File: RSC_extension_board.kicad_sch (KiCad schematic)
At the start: 35 parts, among them J1 Conn_01x03, J10 Conn_01x02, J2 Conn_01x03, J3 Raspberry_Pi_4, J4 Conn_01x04, J5 Conn_01x03, J6 Conn_01x02, J7 Conn_01x03, J8 PRT-14417, J9 USB_C_Receptacle_PowerOnly_6P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

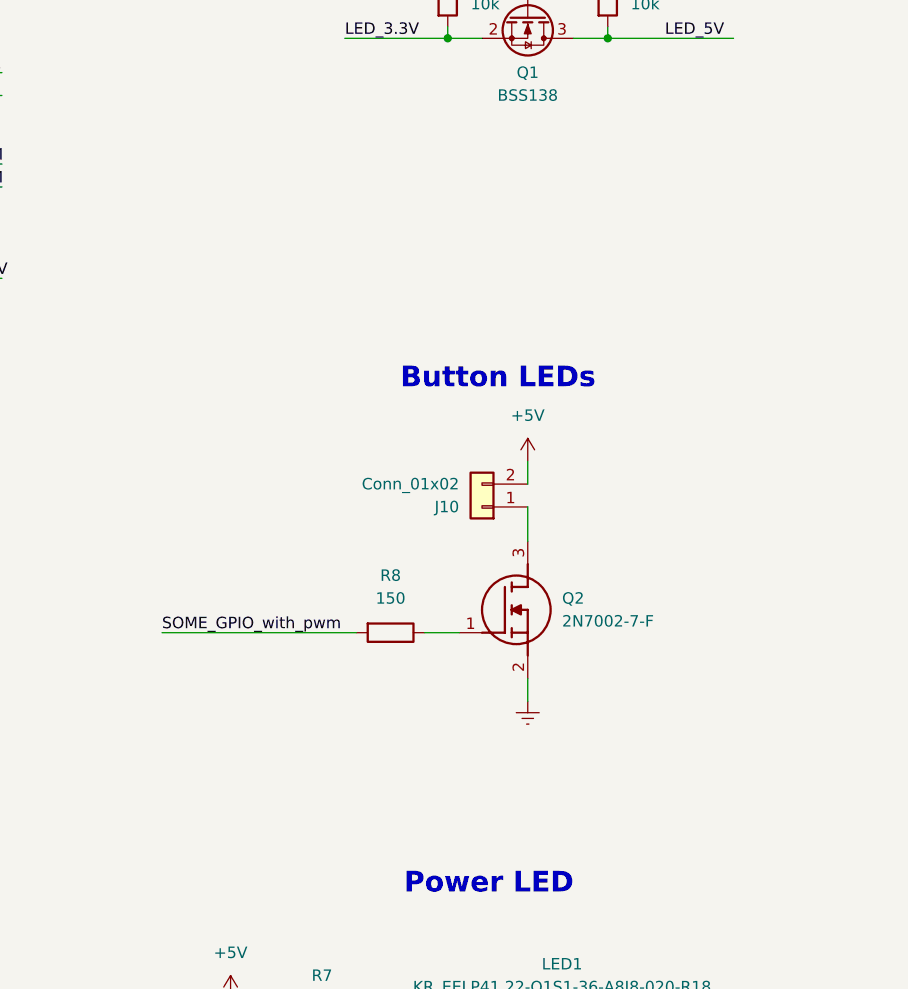
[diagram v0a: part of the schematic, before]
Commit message: started possible voice schematic
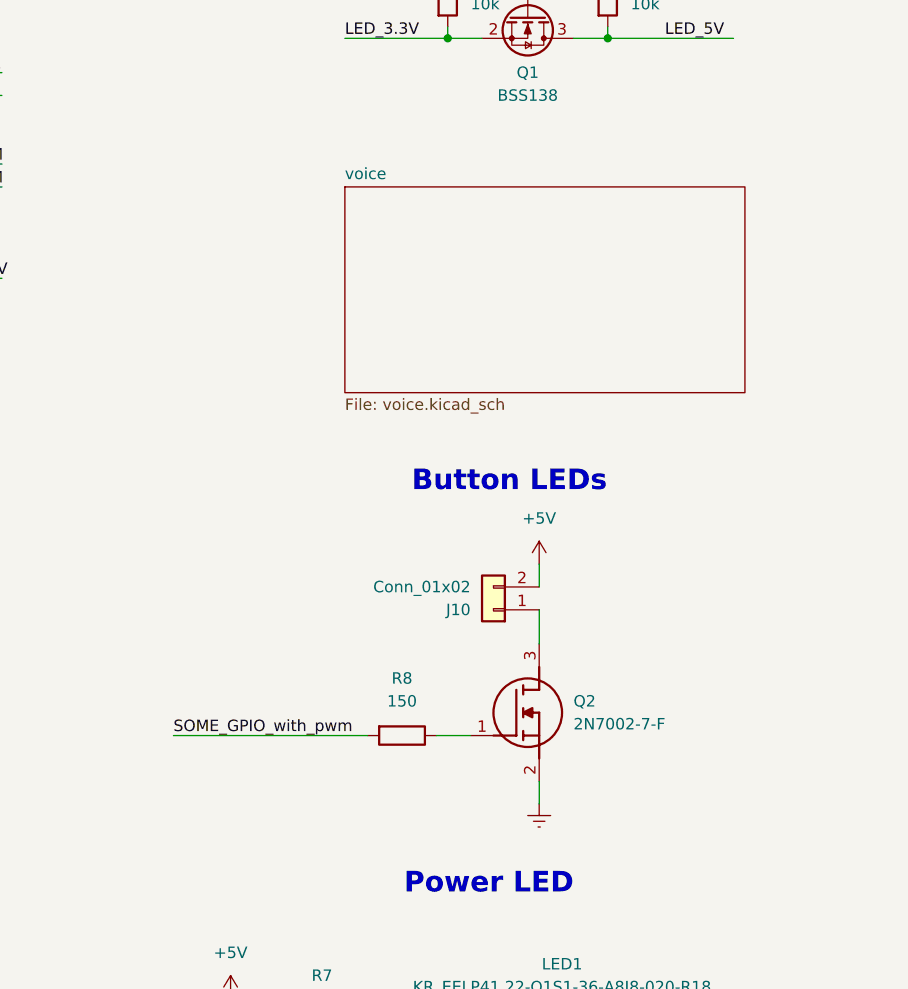
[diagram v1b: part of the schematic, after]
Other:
- added sheet voice (voice.kicad_sch)
- moved on the sheet: J10, Q2, R8
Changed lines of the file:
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@@
 	(text "Button LEDs"
 		(exclude_from_sim no)
-		(at 165.608 82.296 0)
+		(at 166.878 93.726 0)
 		(effects
 			(font
@@
 	(wire
 		(pts
-			(xy 128.27 110.49) (xy 149.86 110.49)
+			(xy 129.54 121.92) (xy 151.13 121.92)
 		)
 		(stroke
@@
 	(wire
 		(pts
-			(xy 157.48 110.49) (xy 161.29 110.49)
+			(xy 158.75 121.92) (xy 162.56 121.92)
 		)
 		(stroke
@@
 	(wire
 		(pts
-			(xy 168.91 96.52) (xy 168.91 100.33)
+			(xy 170.18 107.95) (xy 170.18 111.76)
 		)
 		(stroke
@@
 	(wire
 		(pts
-			(xy 168.91 118.11) (xy 168.91 115.57)
+			(xy 170.18 129.54) (xy 170.18 127)
 		)
 		(stroke
@@
 	(wire
 		(pts
-			(xy 168.91 91.44) (xy 168.91 93.98)
+			(xy 170.18 102.87) (xy 170.18 105.41)
 		)
 		(stroke
@@
 	)
 	(label "SOME_GPIO_with_pwm"
-		(at 128.27 110.49 0)
+		(at 129.54 121.92 0)
 		(effects
 			(font
@@
 	(symbol
 		(lib_id "power:+5V")
-		(at 168.91 91.44 0)
+		(at 170.18 102.87 0)
 		(unit 1)
 		(exclude_from_sim no)
@@
 		(fields_autoplaced yes)
 		(property "Reference" "#PWR032"
-			(at 168.91 95.25 0)
+			(at 170.18 106.68 0)
 			(effects
 				(font
@@
 		)
 		(property "Value" "+5V"
-			(at 168.91 86.36 0)
+			(at 170.18 97.79 0)
 			(effects
 				(font
@@
 		)
 		(property "Footprint" ""
-			(at 168.91 91.44 0)
+			(at 170.18 102.87 0)
 			(effects
 				(font
@@
 		)
 		(property "Datasheet" ""
-			(at 168.91 91.44 0)
+			(at 170.18 102.87 0)
 			(effects
 				(font
@@
 		)
 		(property "Description" "Power symbol creates a global label with name \"+5V\""
-			(at 168.91 91.44 0)
+			(at 170.18 102.87 0)
 			(effects
 				(font
@@
 	(symbol
 		(lib_id "Connector_Generic:Conn_01x02")
-		(at 163.83 96.52 180)
+		(at 165.1 107.95 180)
 		(unit 1)
 		(exclude_from_sim no)
@@
 		(fields_autoplaced yes)
 		(property "Reference" "J10"
-			(at 161.29 96.5201 0)
+			(at 162.56 107.9501 0)
 			(effects
 				(font
@@
 		)
 		(property "Value" "Conn_01x02"
-			(at 161.29 93.9801 0)
+			(at 162.56 105.4101 0)
 			(effects
 				(font
@@
 		)
 		(property "Footprint" "Connector_PinHeader_2.54mm:PinHeader_1x02_P2.54mm_Vertical"
-			(at 163.83 96.52 0)
+			(at 165.1 107.95 0)
 			(effects
 				(font
@@
 		)
 		(property "Datasheet" "~"
-			(at 163.83 96.52 0)
+			(at 165.1 107.95 0)
 			(effects
 				(font
@@
 		)
 		(property "Description" "Generic connector, single row, 01x02, script generated (kicad-library-utils/schlib/autogen/connector/)"
-			(at 163.83 96.52 0)
+			(at 165.1 107.95 0)
 			(effects
 				(font
@@
 	(symbol
 		(lib_id "Device:R")
-		(at 153.67 110.49 270)
+		(at 154.94 121.92 270)
 		(unit 1)
 		(exclude_from_sim no)
@@
 		(fields_autoplaced yes)
 		(property "Reference" "R8"
-			(at 153.67 104.14 90)
+			(at 154.94 115.57 90)
 			(effects
 				(font
@@
 		)
 		(property "Value" "150"
-			(at 153.67 106.68 90)
+			(at 154.94 118.11 90)
 			(effects
 				(font
@@
 		)
 		(property "Footprint" "Resistor_SMD:R_0603_1608Metric_Pad0.98x0.95mm_HandSolder"
-			(at 153.67 108.712 90)
+			(at 154.94 120.142 90)
 			(effects
 				(font
@@
 		)
 		(property "Datasheet" "~"
-			(at 153.67 110.49 0)
+			(at 154.94 121.92 0)
 			(effects
 				(font
@@
 		)
 		(property "Description" "Resistor"
-			(at 153.67 110.49 0)
+			(at 154.94 121.92 0)
 			(effects
 				(font
@@
 	(symbol
 		(lib_id "power:Earth")
-		(at 168.91 118.11 0)
+		(at 170.18 129.54 0)
 		(unit 1)
 		(exclude_from_sim no)
@@
 		(dnp no)
 		(property "Reference" "#PWR031"
-			(at 168.91 124.46 0)
+			(at 170.18 135.89 0)
 			(effects
 				(font
@@
 		)
 		(property "Value" "Earth"
-			(at 162.306 119.634 0)
+			(at 163.576 131.064 0)
 			(effects
 				(font
@@
 		)
 		(property "Footprint" ""
-			(at 168.91 118.11 0)
+			(at 170.18 129.54 0)
 			(effects
 				(font
@@
 		)
 		(property "Datasheet" "~"
-			(at 168.91 118.11 0)
+			(at 170.18 129.54 0)
 			(effects
 				(font
@@
 		)
 		(property "Description" "Power symbol creates a global label with name \"Earth\""
-			(at 168.91 118.11 0)
+			(at 170.18 129.54 0)
 			(effects
 				(font
@@
 	(symbol
 		(lib_id "2N7002-7-F:2N7002-7-F")
-		(at 161.29 110.49 0)
+		(at 162.56 121.92 0)
 		(unit 1)
 		(exclude_from_sim no)
@@
 		(fields_autoplaced yes)
 		(property "Reference" "Q2"
-			(at 172.72 106.6799 0)
+			(at 173.99 118.1099 0)
 			(effects
 				(font
@@
 		)
 		(property "Value" "2N7002-7-F"
-			(at 172.72 109.2199 0)
+			(at 173.99 120.6499 0)
 			(effects
 				(font
@@
 		)
 		(property "Footprint" "2N7002-7-F:SOT96P240X120-3N"
-			(at 172.72 209.22 0)
+			(at 173.99 220.65 0)
 			(effects
 				(font
@@
 		)
 		(property "Datasheet" "https://datasheet.datasheetarchive.com/originals/distributors/SFDatasheet-0/sf-0003625.pdf"
-			(at 172.72 309.22 0)
+			(at 173.99 320.65 0)
 			(effects
 				(font
@@
 		)
 		(property "Description" "MOSFET N-Channel 60V 0.21A SOT23 Diodes Inc 2N7002-7-F N-channel MOSFET Transistor, 0.115 A, 60 V, 3-Pin SOT-23"
-			(at 161.29 110.49 0)
+			(at 162.56 121.92 0)
 			(effects
 				(font
@@
 		)
 		(property "Height" "1.2"
-			(at 172.72 509.22 0)
+			(at 173.99 520.65 0)
 			(effects
 				(font
@@
 		)
 		(property "Manufacturer_Name" "Diodes Incorporated"
-			(at 172.72 609.22 0)
+			(at 173.99 620.65 0)
 			(effects
 				(font
@@
 		)
 		(property "Manufacturer_Part_Number" "2N7002-7-F"
-			(at 172.72 709.22 0)
+			(at 173.99 720.65 0)
 			(effects
 				(font
@@
 		)
 		(property "Mouser Part Number" "621-2N7002-F"
-			(at 172.72 809.22 0)
+			(at 173.99 820.65 0)
 			(effects
 				(font
@@
 		)
 		(property "Mouser Price/Stock" "https://www.mouser.co.uk/ProductDetail/Diodes-Incorporated/2N7002-7-F?qs=jMXWnm70%252BC%252BAX%252BMLzUkTZg%3D%3D"
-			(at 172.72 909.22 0)
+			(at 173.99 920.65 0)
 			(effects
 				(font
@@
 		)
 		(property "Arrow Part Number" "2N7002-7-F"
-			(at 172.72 1009.22 0)
+			(at 173.99 1020.65 0)
 			(effects
 				(font
@@
 		)
 		(property "Arrow Price/Stock" "https://www.arrow.com/en/products/2n7002-7-f/diodes-incorporated?utm_currency=USD&region=europe"
-			(at 172.72 1109.22 0)
+			(at 173.99 1120.65 0)
 			(effects
 				(font
@@
 				)
 			)
+		)
+	)
+	(sheet
+		(at 148.59 60.96)
+		(size 44.45 22.86)
+		(exclude_from_sim no)
+		(in_bom yes)
+		(on_board yes)
+		(dnp no)
+		(fields_autoplaced yes)
+		(stroke
+			(width 0.1524)
+			(type solid)
+		)
+		(fill
+			(color 0 0 0 0.0000)
+		)
+		(property "Sheetname" "voice"
+			(at 148.59 60.2484 0)
+			(effects
+				(font
+					(size 1.27 1.27)
+				)
+				(justify left bottom)
+			)
+		)
+		(property "Sheetfile" "voice.kicad_sch"
+			(at 148.59 84.4046 0)
+			(effects
+				(font
+					(size 1.27 1.27)
+				)
+				(justify left top)
+			)
+		)
+		(instances
+			(project "RSC_extension_board"
+				(path "/1f48ed4c-84ce-4e77-88fc-25bf92dcee2d"
+					(page "2")
+				)
+			)

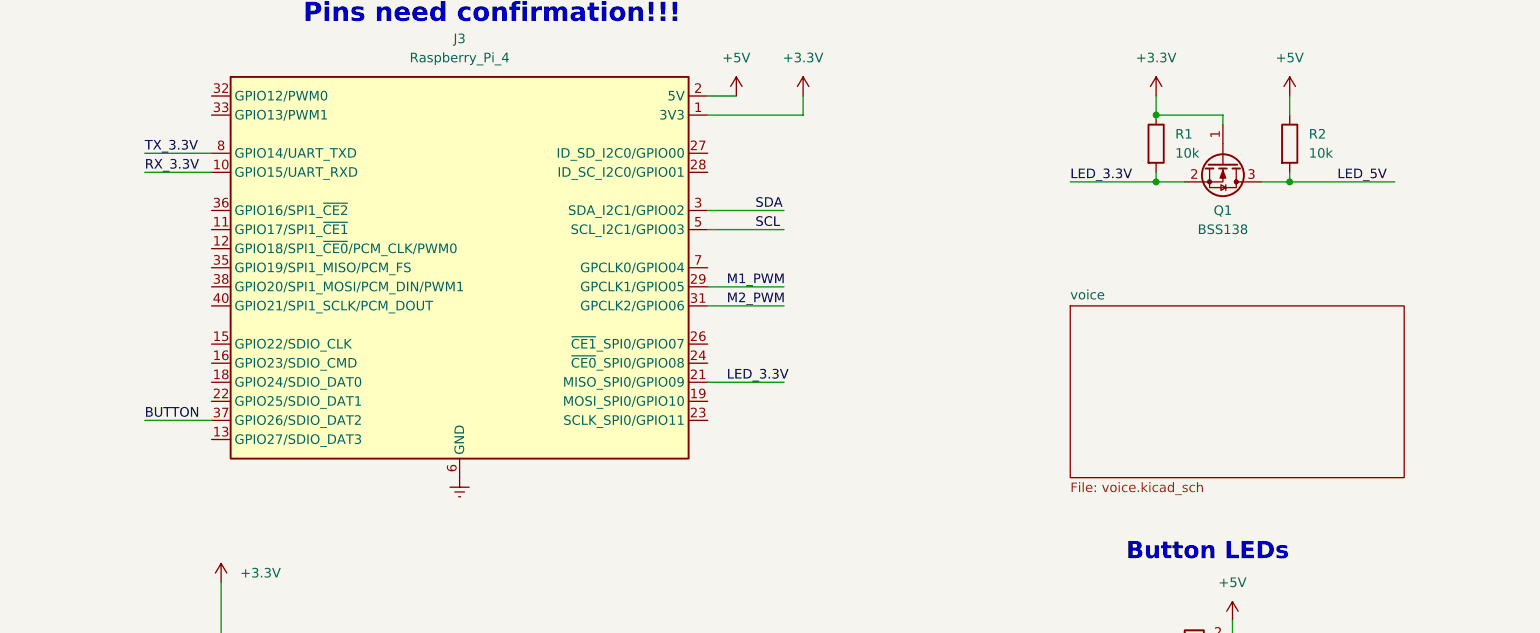
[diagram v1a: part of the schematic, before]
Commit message: voice schematic switch, 3d files
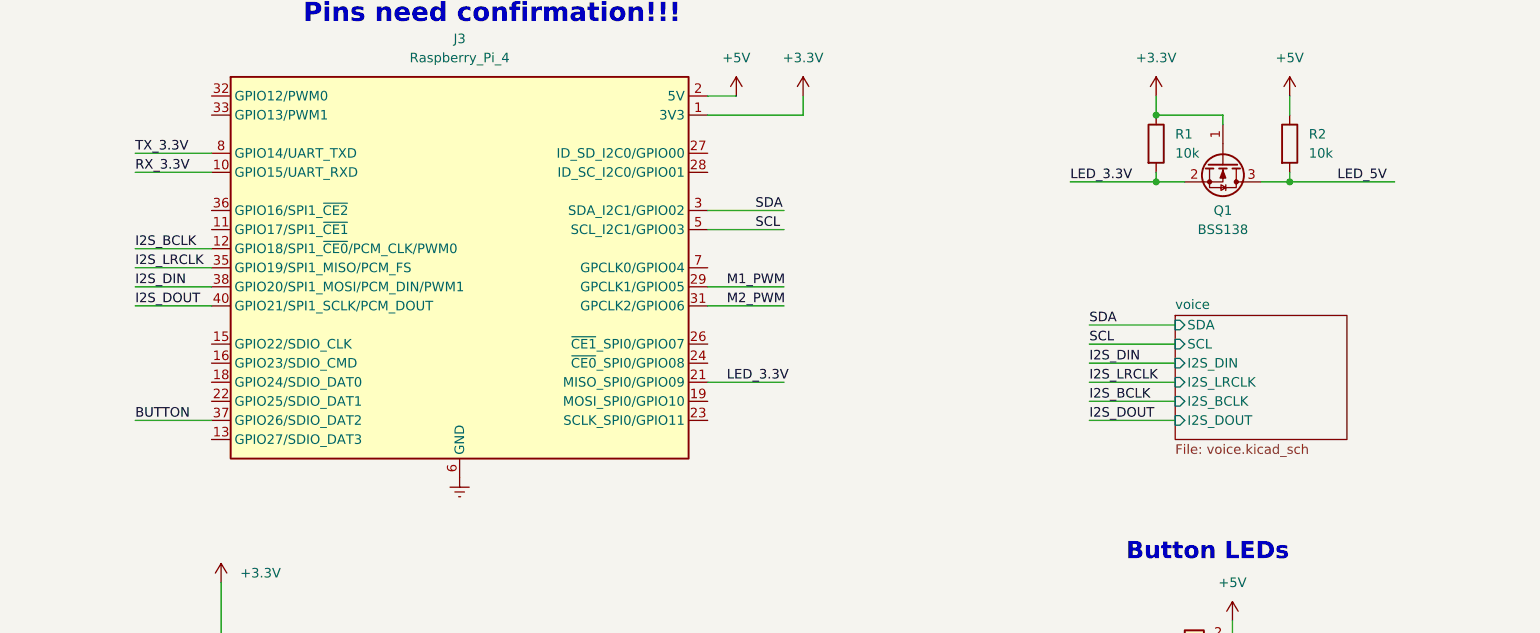
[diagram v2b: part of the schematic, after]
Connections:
- net I2S_BCLK: now reaches J3.12 (GPIO18/SPI1_~{CE0}/PCM_CLK/PWM0)
- net I2S_LRCLK: now reaches J3.35 (GPIO19/SPI1_MISO/PCM_FS)
- net I2S_DIN: now reaches J3.38 (GPIO20/SPI1_MOSI/PCM_DIN/PWM1)
- net I2S_DOUT: now reaches J3.40 (GPIO21/SPI1_SCLK/PCM_DOUT)
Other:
- sheet voice ports: added I2S_BCLK, I2S_DIN, I2S_DOUT, I2S_LRCLK, SCL, SDA; removed none

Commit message: a4 to a3
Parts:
- added C35: 100nF, Capacitor_SMD:C_0603_1608Metric_Pad1.08x0.95mm_HandSolder, symbol Device:C
- added J13: Conn_01x03, Connector_PinHeader_2.54mm:PinHeader_1x03_P2.54mm_Horizontal, symbol Connector_Generic:Conn_01x03
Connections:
- net +5V: now also J10.1 (Pin_1), C35.1, J13.2 (Pin_2); no longer J10.2 (Pin_2)
- net Earth: now also C35.2, J13.3 (Pin_3)
- net at Q2.3 (D): now also J10.2 (Pin_2); no longer J10.1 (Pin_1)
- net SOME_GPIO_with_pwm renamed LED_PWM
- new net M3_PWM: J13.1 (Pin_1)
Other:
- moved on the sheet: C1, C2, C3, C4, C5, C6, C7, D1, D2, D3, F1, J1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

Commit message: some new pins for raspberry gpio-s
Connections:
- net BUTTON: now also J3.16 (GPIO23/SDIO_CMD); no longer J3.37 (GPIO26/SDIO_DAT2)
- net LED_3.3V: no longer J3.21 (MISO_SPI0/GPIO09)
- net LED_PWM: now also J3.18 (GPIO24/SDIO_DAT0)
- net M1_PWM: now also J3.32 (GPIO12/PWM0); no longer J3.29 (GPCLK1/GPIO05)
- net M2_PWM: now also J3.33 (GPIO13/PWM1); no longer J3.31 (GPCLK2/GPIO06)
- net M3_PWM: now also J3.37 (GPIO26/SDIO_DAT2)
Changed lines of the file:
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@@
+	(wire
+		(pts
+			(xy 29.21 73.66) (xy 39.37 73.66)
+		)
+		(stroke
+			(width 0)
+			(type default)
+		)
+	)
 	(wire
 		(pts
@@
 	(wire
 		(pts
-			(xy 105.41 68.58) (xy 115.57 68.58)
-		)
-		(stroke
-			(width 0)
-			(type default)
-		)
-	)
-	(wire
-		(pts
 			(xy 350.52 69.85) (xy 358.14 69.85)
 		)
@@
 	(wire
 		(pts
-			(xy 105.41 55.88) (xy 115.57 55.88)
-		)
-		(stroke
-			(width 0)
-			(type default)
-		)
-	)
-	(wire
-		(pts
 			(xy 73.66 161.29) (xy 85.09 161.29)
 		)
@@
 	(wire
 		(pts
+			(xy 29.21 30.48) (xy 39.37 30.48)
+		)
+		(stroke
+			(width 0)
+			(type default)
+		)
+	)
+	(wire
+		(pts
 			(xy 346.71 182.88) (xy 370.84 182.88)
 		)
@@
 	(wire
 		(pts
+			(xy 29.21 33.02) (xy 39.37 33.02)
+		)
+		(stroke
+			(width 0)
+			(type default)
+		)
+	)
+	(wire
+		(pts
 			(xy 85.09 161.29) (xy 85.09 163.83)
 		)
@@
 	(wire
 		(pts
-			(xy 105.41 58.42) (xy 115.57 58.42)
-		)
-		(stroke
-			(width 0)
-			(type default)
-		)
-	)
-	(wire
-		(pts
 			(xy 346.71 48.26) (xy 346.71 44.45)
 		)
@@
 	(wire
 		(pts
-			(xy 29.21 73.66) (xy 39.37 73.66)
-		)
-		(stroke
-			(width 0)
-			(type default)
-		)
-	)
-	(wire
-		(pts
 			(xy 97.79 118.11) (xy 97.79 119.38)
 		)
@@
 	(wire
 		(pts
+			(xy 29.21 68.58) (xy 39.37 68.58)
+		)
+		(stroke
+			(width 0)
+			(type default)
+		)
+	)
+	(wire
+		(pts
 			(xy 346.71 172.72) (xy 346.71 175.26)
 		)
@@
 	(wire
 		(pts
+			(xy 29.21 66.04) (xy 39.37 66.04)
+		)
+		(stroke
+			(width 0)
+			(type default)
+		)
+	)
+	(wire
+		(pts
 			(xy 346.71 154.94) (xy 370.84 154.94)
 		)
@@
 		)
 	)
-	(label "M2_PWM"
-		(at 107.95 58.42 0)
-		(effects
-			(font
-				(size 1.27 1.27)
-			)
-			(justify left bottom)
-		)
-	)
-	(label "BUTTON"
-		(at 29.21 73.66 0)
+	(label "LED_PWM"
+		(at 29.21 68.58 0)
 		(effects
 			(font
@@
 		)
 	)
-	(label "M3_PWM"
-		(at 121.92 57.15 0)
-		(effects
-			(font
-				(size 1.27 1.27)
-			)
-			(justify left bottom)
-		)
-	)
 	(label "LED_PWM"
 		(at 175.26 125.73 0)
@@
 		)
 	)
+	(label "LED_3.3V"
+		(at 118.11 76.2 0)
+		(effects
+			(font
+				(size 1.27 1.27)
+			)
+			(justify left bottom)
+		)
+	)
 	(label "I2S_DIN"
 		(at 29.21 55.88 0)
@@
 		)
 	)
-	(label "LED_3.3V"
-		(at 107.95 68.58 0)
-		(effects
-			(font
-				(size 1.27 1.27)
-			)
-			(justify left bottom)
-		)
-	)
 	(label "I2S_LRCLK"
 		(at 186.69 74.93 0)
@@
 		)
 	)
+	(label "M2_PWM"
+		(at 29.21 33.02 0)
+		(effects
+			(font
+				(size 1.27 1.27)
+			)
+			(justify left bottom)
+		)
+	)
 	(label "I2S_BCLK"
 		(at 186.69 77.47 0)
@@
 		)
 	)
+	(label "M1_PWM"
+		(at 29.21 30.48 0)
+		(effects
+			(font
+				(size 1.27 1.27)
+			)
+			(justify left bottom)
+		)
+	)
 	(label "SCL"
 		(at 350.52 204.47 0)
@@
 		)
 	)
-	(label "M1_PWM"
-		(at 107.95 55.88 0)
+	(label "BUTTON"
+		(at 29.21 66.04 0)
 		(effects
 			(font
@@
 		)
 	)
-	(label "LED_PWM"
-		(at 125.73 60.96 0)
-		(effects
-			(font
-				(size 1.27 1.27)
-			)
-			(justify left bottom)
-		)
-	)
 	(label "TX_3.3V"
 		(at 29.21 38.1 0)
 		(effects
 			(font
+				(size 1.27 1.27)
+			)
+			(justify left bottom)
+		)
+	)
+	(label "M3_PWM"
+		(at 29.21 73.66 0)
+		(effects
+			(font

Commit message: Led_3.3 has also net
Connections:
- net LED_3.3V: now also J3.31 (GPCLK2/GPIO06)
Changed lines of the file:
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@@
+	(wire
+		(pts
+			(xy 105.41 58.42) (xy 115.57 58.42)
+		)
+		(stroke
+			(width 0)
+			(type default)
+		)
+	)
 	(wire
 		(pts
@@
 		)
 	)
+	(label "LED_3.3V"
+		(at 107.95 58.42 0)
+		(effects
+			(font
+				(size 1.27 1.27)
+			)
+			(justify left bottom)
+		)
+	)
 	(label "SDA"
 		(at 186.69 67.31 0)
@@
 		(effects
 			(font
-				(size 1.27 1.27)
-			)
-			(justify left bottom)
-		)
-	)
-	(label "LED_3.3V"
-		(at 118.11 76.2 0)
-		(effects
-			(font

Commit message: new power switch, added spi out
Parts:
- removed SW1: SW_Wuerth_450301014042, Button_Switch_THT:SW_Slide-03_Wuerth-WS-SLTV_10x2.5x6.4_P2.54mm, symbol Switch:SW_Wuerth_450301014042
- added J14: 500SSP1S2M2QEA, 500SSP1S2M2QEA, symbol 500SSP1S2M2QEA:500SSP1S2M2QEA
- added J15: Conn_01x05, Connector_PinSocket_2.54mm:PinSocket_1x05_P2.54mm_Vertical, symbol Connector_Generic:Conn_01x05
- J9: footprint Connector_USB:USB_C_Receptacle_GCT_USB4125-xx-x_6P_TopMnt_Horizontal -> Connector_USB:USB_C_Receptacle_GCT_USB4125-xx-x-0190_6P_TopMnt_Horizontal
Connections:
- net +5V: now also J14.3
- net GPIO10: now reaches J3.19 (MOSI_SPI0/GPIO10)
- net GPIO10: now also J15.4 (Pin_4)
- net GPIO09: now reaches J3.21 (MISO_SPI0/GPIO09)
- net GPIO09: now also J15.3 (Pin_3)
- net GPIO11: now reaches J3.23 (SCLK_SPI0/GPIO11)
- net GPIO11: now also J15.5 (Pin_5)
- net GPIO08: now reaches J3.24 (~{CE0}_SPI0/GPIO08)
- net GPIO08: now also J15.2 (Pin_2)
- net GPIO07: now reaches J3.26 (~{CE1}_SPI0/GPIO07)
- net GPIO07: now also J15.1 (Pin_1)
- net at F1.2: now also J14.2
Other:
- note added: "Any more pins needed for spi display? Pin order?"
- note added: "SPI"
- note removed: "right now power. maybe later battery things?"
- moved on the sheet: C1, C2, C3, C35, C4, C6, J1, J13, J2, J4, J5, J7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

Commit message: added power for spi
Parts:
- removed J15: Conn_01x05, Connector_PinSocket_2.54mm:PinSocket_1x05_P2.54mm_Vertical, symbol Connector_Generic:Conn_01x05
- added C36: 100nF, Capacitor_SMD:C_0603_1608Metric_Pad1.08x0.95mm_HandSolder, symbol Device:C
- added J16: Conn_01x07, Connector_PinSocket_2.54mm:PinSocket_1x07_P2.54mm_Vertical, symbol Connector_Generic:Conn_01x07
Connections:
- net +3.3V: now also C36.1, J16.1 (Pin_1)
- net Earth: now also C36.2, J16.2 (Pin_2)
- net GPIO07: now also J16.3 (Pin_3)
- net GPIO08: now also J16.4 (Pin_4)
- net GPIO09: now also J16.5 (Pin_5)
- net GPIO10: now also J16.6 (Pin_6)
- net GPIO11: now also J16.7 (Pin_7)
